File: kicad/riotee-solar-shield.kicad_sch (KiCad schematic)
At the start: 7 parts, among them J1 Conn_01x10, J2 Conn_01x12, SW1 SW_DIP_x02

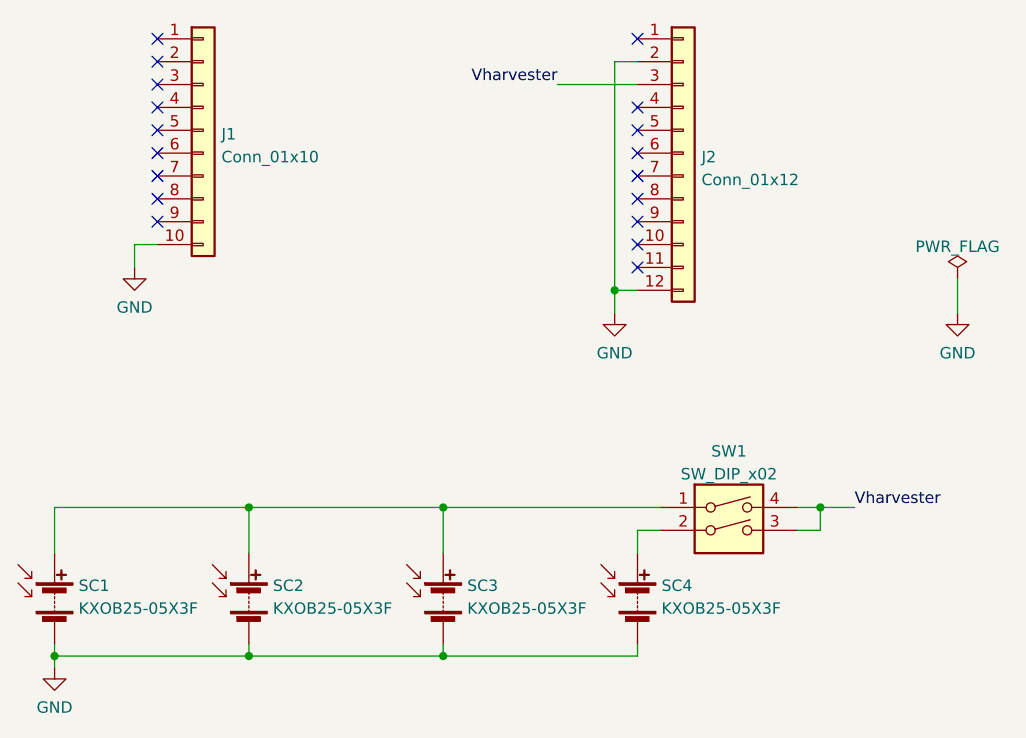
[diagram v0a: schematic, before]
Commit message: Switch to  KXOB25-03x4F and update to KiCad 9
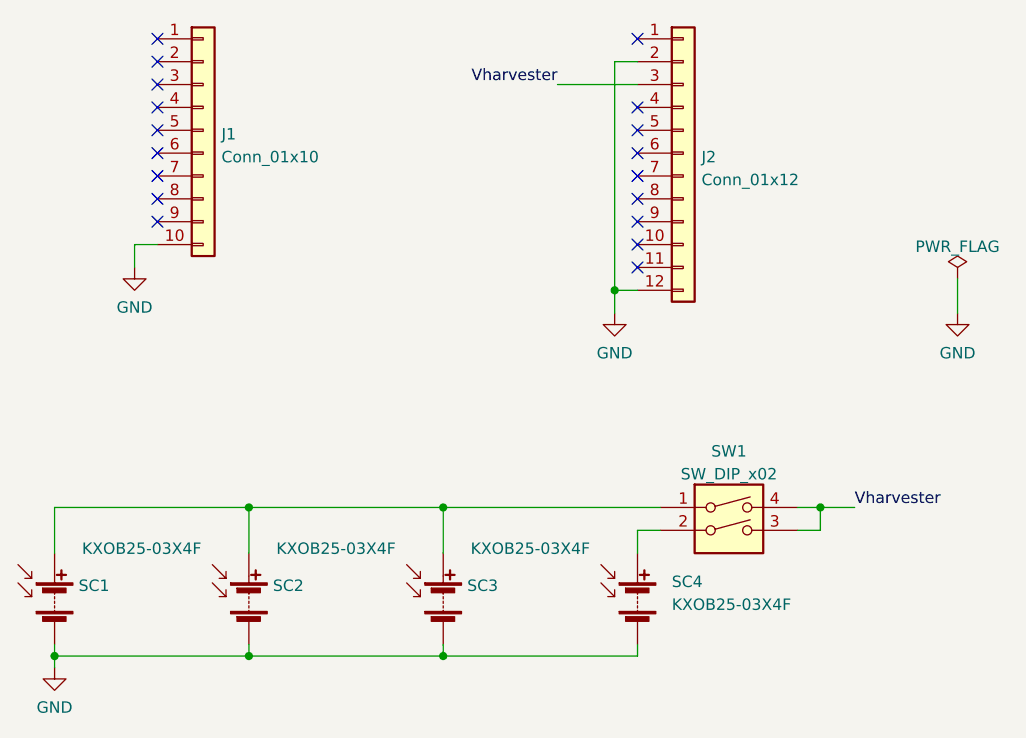
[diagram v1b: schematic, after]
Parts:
- SC1, SC2, SC3, SC4: value KXOB25-05X3F -> KXOB25-03X4F; symbol riotee:KXOB25-05X3F -> riotee:KXOB25-03X4F; MPN KXOB25-05X3F-TR -> KXOB25-03X4F-TR
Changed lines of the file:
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@@
 (kicad_sch
-	(version 20231120)
+	(version 20250114)
 	(generator "eeschema")
-	(generator_version "8.0")
+	(generator_version "9.0")
 	(paper "A4")
 	(junction
@@
 	(label "Vharvester"
 		(at 163.83 48.26 180)
-		(fields_autoplaced yes)
 		(effects
 			(font
@@
 	(label "Vharvester"
 		(at 196.85 95.25 0)
-		(fields_autoplaced yes)
 		(effects
 			(font
@@
 	)
 	(symbol
-		(lib_id "riotee:KXOB25-05X3F")
+		(lib_id "riotee:KXOB25-03X4F")
 		(at 172.72 105.41 0)
 		(unit 1)
@@
 		(fields_autoplaced yes)
 		(property "Reference" "SC4"
-			(at 175.387 103.9403 0)
+			(at 176.53 103.5049 0)
 			(effects
 				(font
@@
 			)
 		)
-		(property "Value" "KXOB25-05X3F"
-			(at 175.387 106.4772 0)
+		(property "Value" "KXOB25-03X4F"
+			(at 176.53 106.0449 0)
 			(effects
 				(font
@@
 			)
 		)
-		(property "Datasheet" "https://waf-e.dubudisk.com/anysolar.dubuplus.com/techsupport@anysolar.biz/O18Ae07/DubuDisk/www/Gen3/KXOB25-05X3F%20DATA%20SHEET%20202007.pdf"
+		(property "Datasheet" "https://waf-e.dubudisk.com/anysolar.dubuplus.com/techsupport@anysolar.biz/O18Ae07/DubuDisk/www/Gen3/KXOB25-03X4F%20DATA%20SHEET%20202007.pdf"
 			(at 176.53 118.11 0)
 			(effects
@@
 			)
 		)
-		(property "MPN" "KXOB25-05X3F-TR"
+		(property "MPN" "KXOB25-03X4F-TR"
 			(at 172.72 105.41 0)
 			(effects
@@
 	)
 	(symbol
-		(lib_id "riotee:KXOB25-05X3F")
+		(lib_id "riotee:KXOB25-03X4F")
 		(at 129.54 105.41 0)
 		(unit 1)
@@
 			)
 		)
-		(property "Value" "KXOB25-05X3F"
-			(at 132.207 106.4772 0)
+		(property "Value" "KXOB25-03X4F"
+			(at 132.588 99.822 0)
 			(effects
 				(font
@@
 			)
 		)
-		(property "Datasheet" "https://waf-e.dubudisk.com/anysolar.dubuplus.com/techsupport@anysolar.biz/O18Ae07/DubuDisk/www/Gen3/KXOB25-05X3F%20DATA%20SHEET%20202007.pdf"
+		(property "Datasheet" "https://waf-e.dubudisk.com/anysolar.dubuplus.com/techsupport@anysolar.biz/O18Ae07/DubuDisk/www/Gen3/KXOB25-03X4F%20DATA%20SHEET%20202007.pdf"
 			(at 133.35 118.11 0)
 			(effects
@@
 			)
 		)
-		(property "MPN" "KXOB25-05X3F-TR"
+		(property "MPN" "KXOB25-03X4F-TR"
 			(at 129.54 105.41 0)
 			(effects
@@
 	)
 	(symbol
-		(lib_id "riotee:KXOB25-05X3F")
+		(lib_id "riotee:KXOB25-03X4F")
 		(at 107.95 105.41 0)
 		(unit 1)
@@
 			)
 		)
-		(property "Value" "KXOB25-05X3F"
-			(at 110.617 106.4772 0)
+		(property "Value" "KXOB25-03X4F"
+			(at 110.998 99.822 0)
 			(effects
 				(font
@@
 			)
 		)
-		(property "Datasheet" "https://waf-e.dubudisk.com/anysolar.dubuplus.com/techsupport@anysolar.biz/O18Ae07/DubuDisk/www/Gen3/KXOB25-05X3F%20DATA%20SHEET%20202007.pdf"
+		(property "Datasheet" "https://waf-e.dubudisk.com/anysolar.dubuplus.com/techsupport@anysolar.biz/O18Ae07/DubuDisk/www/Gen3/KXOB25-03X4F%20DATA%20SHEET%20202007.pdf"
 			(at 111.76 118.11 0)
 			(effects
@@
 			)
 		)
-		(property "MPN" "KXOB25-05X3F-TR"
+		(property "MPN" "KXOB25-03X4F-TR"
 			(at 107.95 105.41 0)
 			(effects
@@
 	)
 	(symbol
-		(lib_id "riotee:KXOB25-05X3F")
+		(lib_id "riotee:KXOB25-03X4F")
 		(at 151.13 105.41 0)
 		(unit 1)
@@
 			)
 		)
-		(property "Value" "KXOB25-05X3F"
-			(at 153.797 106.4772 0)
+		(property "Value" "KXOB25-03X4F"
+			(at 154.178 99.822 0)
 			(effects
 				(font
@@
 			)
 		)
-		(property "Datasheet" "https://waf-e.dubudisk.com/anysolar.dubuplus.com/techsupport@anysolar.biz/O18Ae07/DubuDisk/www/Gen3/KXOB25-05X3F%20DATA%20SHEET%20202007.pdf"
+		(property "Datasheet" "https://waf-e.dubudisk.com/anysolar.dubuplus.com/techsupport@anysolar.biz/O18Ae07/DubuDisk/www/Gen3/KXOB25-03X4F%20DATA%20SHEET%20202007.pdf"
 			(at 154.94 118.11 0)
 			(effects
@@
 			)
 		)
-		(property "MPN" "KXOB25-05X3F-TR"
+		(property "MPN" "KXOB25-03X4F-TR"
 			(at 151.13 105.41 0)
 			(effects
@@
 		)
 	)
+	(embedded_fonts no)
 )
